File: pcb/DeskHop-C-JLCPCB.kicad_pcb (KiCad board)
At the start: 2 copper layers, 66.9 x 74.5 mm, 94 parts, among them J201 Debug, J202 Computer, J203 Power, J204 Device, J301 Debug, J302 Computer, J303 Power, J304 Device, Q201 USB Power Switch, Q301 USB Power Switch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

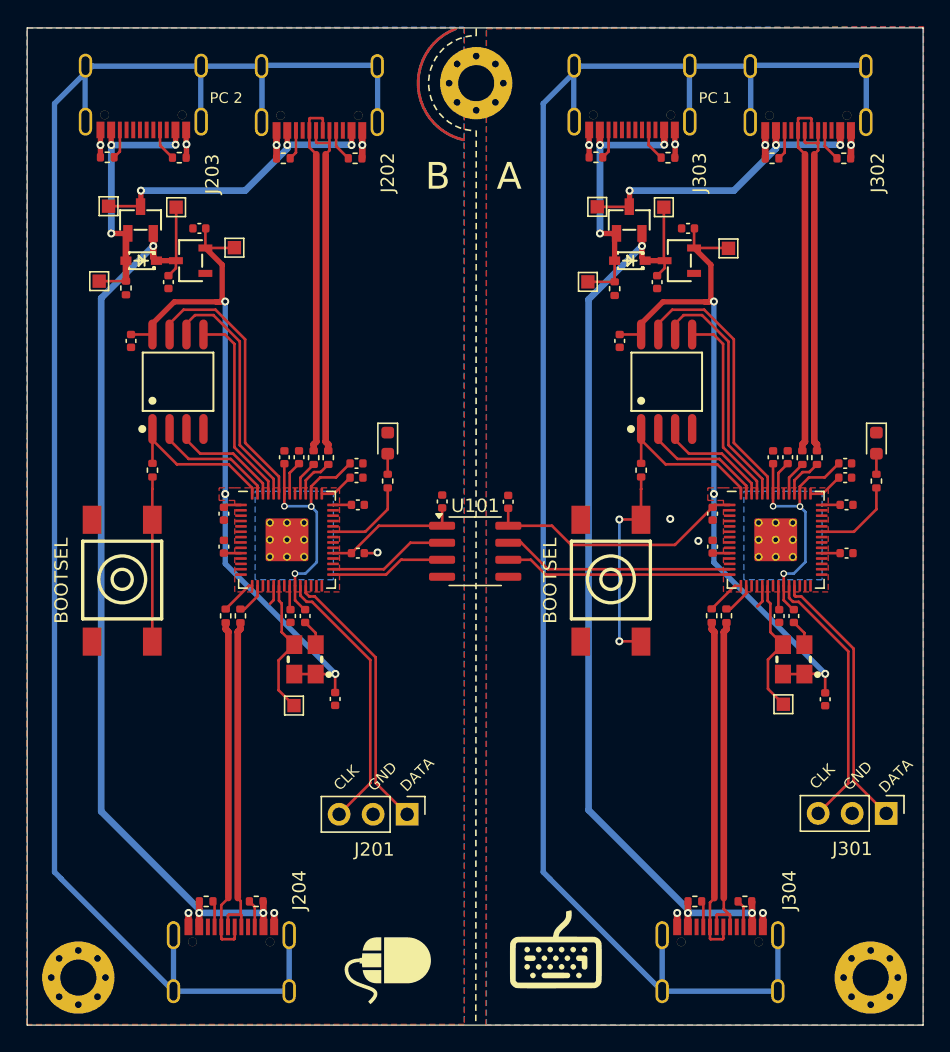
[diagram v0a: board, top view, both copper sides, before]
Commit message: Relocate various items to improve silkscreen placement.
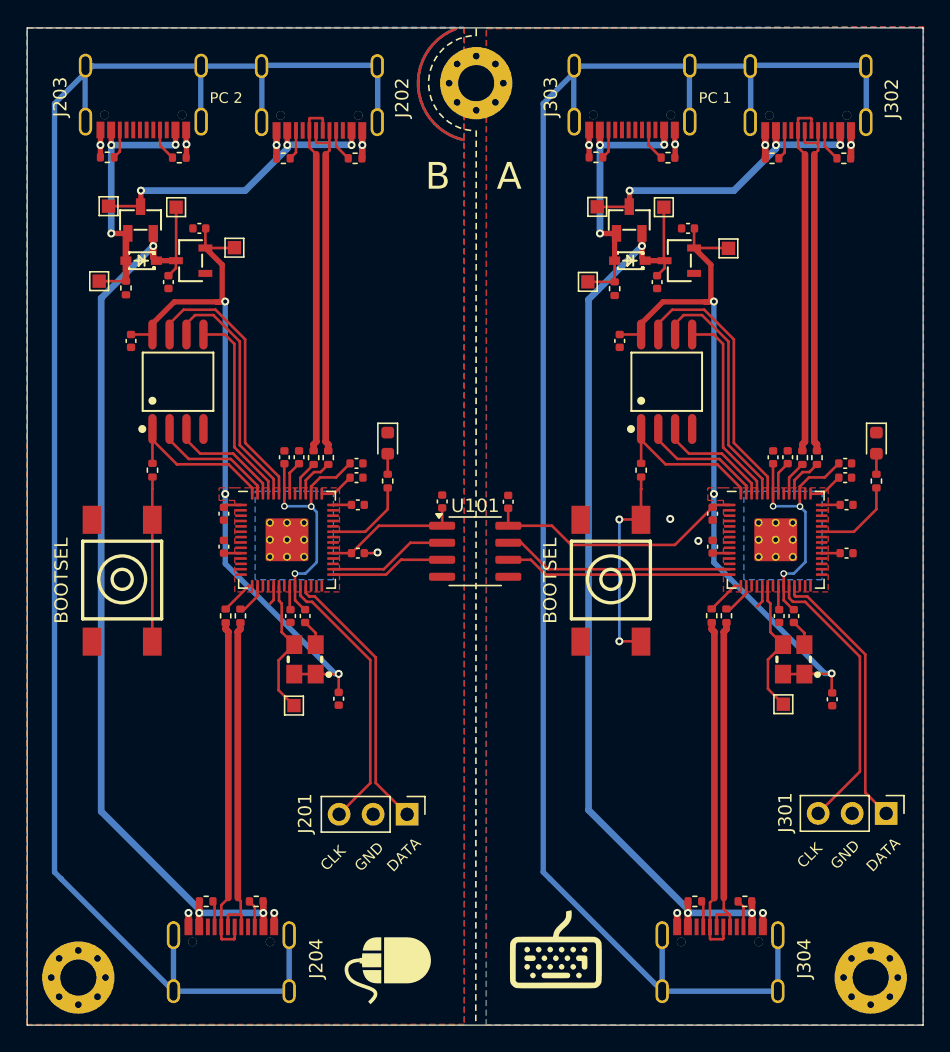
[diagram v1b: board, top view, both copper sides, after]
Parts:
- moved C302 0.53 mm to (93.9, 91.2)
- moved C202 0.27 mm to (57.0, 91.2)
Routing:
- net /Core Right (A)/3V3: track 82.6 -> 83.6 mm
- net Net-(J301-Pin_3): track 20.0 -> 21.0 mm

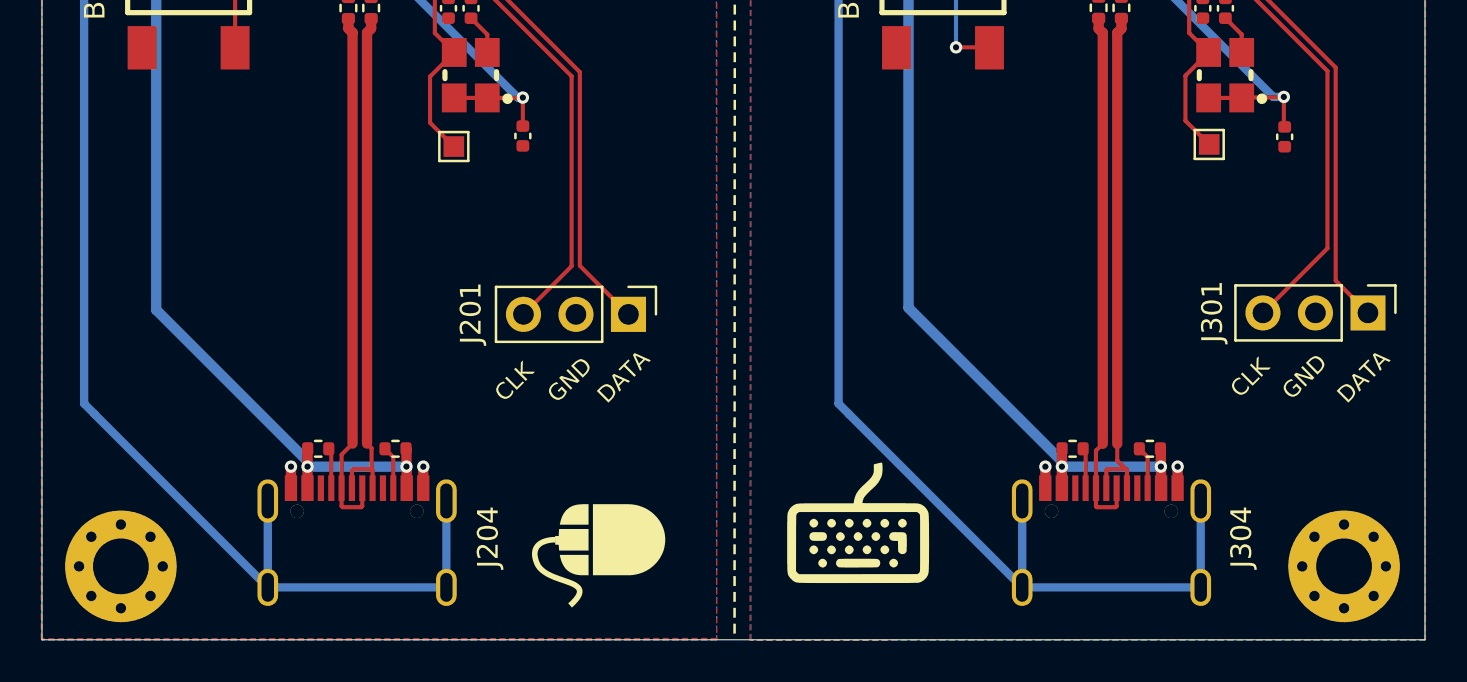
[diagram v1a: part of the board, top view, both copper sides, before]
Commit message: Adjust mounting hole positions to match original board.
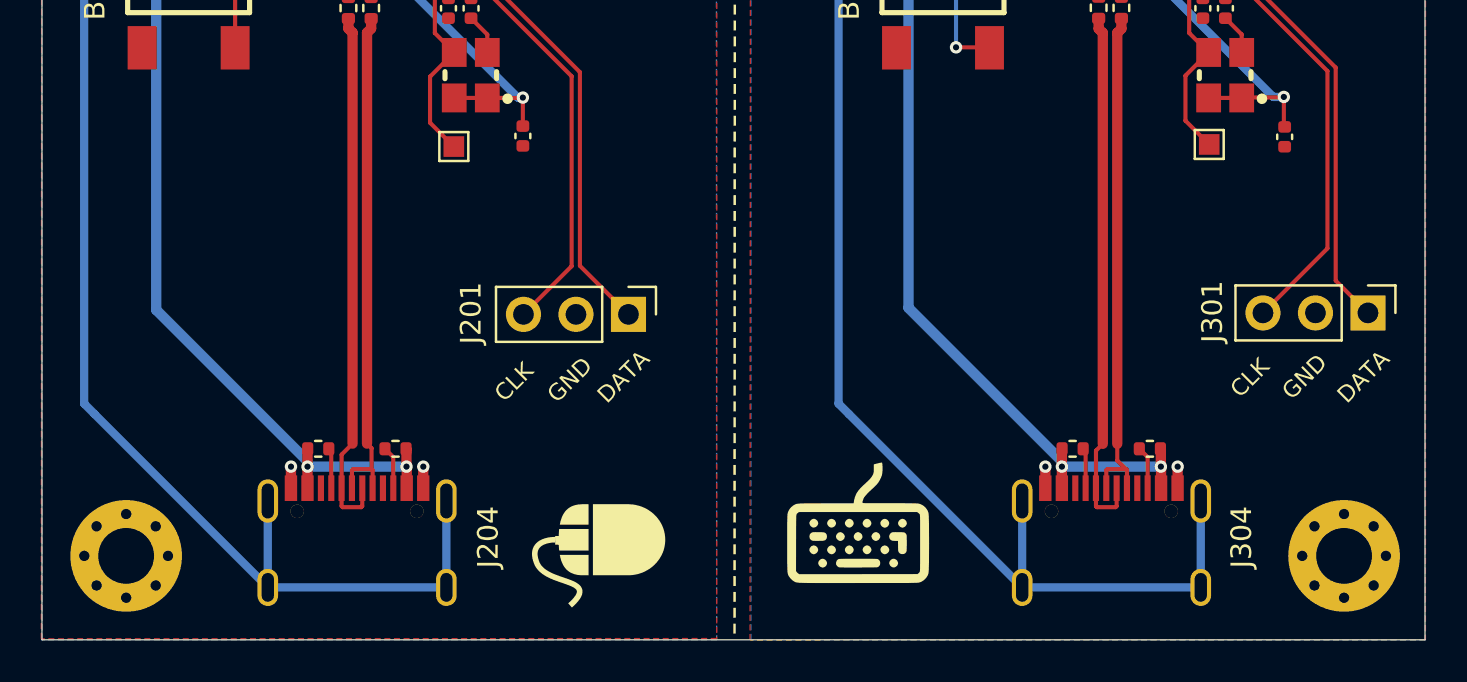
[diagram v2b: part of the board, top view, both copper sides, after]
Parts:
- moved H102 0.57 mm to (37.8, 111.5)
- moved H103 0.51 mm to (96.8, 111.5)
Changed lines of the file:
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@@
   )
   (footprint "MountingHole:MountingHole_2.7mm_M2.5_Pad_Via" (layer "F.Cu")
-    (at 37.592 112.014)
+    (at 37.846 111.506)
     (descr "Mounting Hole 2.7mm")
     (tags "mounting hole 2.7mm")
@@
   )
   (footprint "MountingHole:MountingHole_2.7mm_M2.5_Pad_Via" (layer "F.Cu")
-    (at 96.774 112.014)
+    (at 96.774 111.506)
     (descr "Mounting Hole 2.7mm")
     (tags "mounting hole 2.7mm")
@@
   (segment (start 93.1159 80.3157) (end 94.3805 80.3157) (width 0.2) (layer "F.Cu") (net 3))
   (segment (start 86.2409 80.3157) (end 84.9667 80.3157) (width 0.2) (layer "F.Cu") (net 3))
-  (segment (start 93.86 90.71) (end 93.9 90.75) (width 0.2) (layer "F.Cu") (net 3))
   (segment (start 86.2409 76.7157) (end 85.1359 76.7157) (width 0.2) (layer "F.Cu") (net 3))
   (segment (start 69.7 76.96) (end 69.7 78.2598) (width 0.2) (layer "F.Cu") (net 3))

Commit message: Use better net labels for UART links.
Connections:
- net /Core Left (B)/UART-RX-A renamed /Core Left (B)/RIGHT-UART-RX
- net /Core Left (B)/UART-RX-B renamed /Core Left (B)/LEFT-UART-RX
- net /Core Left (B)/UART-TX-A renamed /Core Left (B)/RIGHT-UART-TX
- net /Core Left (B)/UART-TX-B renamed /Core Left (B)/LEFT-UART-TX
- net /Core Right (A)/UART-RX-A renamed /Core Right (A)/RIGHT-UART-RX
- net /Core Right (A)/UART-RX-B renamed /Core Right (A)/LEFT-UART-RX
- net /Core Right (A)/UART-TX-A renamed /Core Right (A)/RIGHT-UART-TX
- net /Core Right (A)/UART-TX-B renamed /Core Right (A)/LEFT-UART-TX
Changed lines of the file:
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@@
   (net 59 "Net-(U303-GPIO13)")
   (net 60 "Net-(U303-GPIO12)")
-  (net 61 "/Core Left (B)/UART-RX-B")
-  (net 62 "/Core Left (B)/UART-TX-B")
-  (net 63 "/Core Right (A)/UART-RX-A")
-  (net 64 "/Core Right (A)/UART-TX-A")
+  (net 61 "/Core Left (B)/LEFT-UART-RX")
+  (net 62 "/Core Left (B)/LEFT-UART-TX")
+  (net 63 "/Core Right (A)/RIGHT-UART-RX")
+  (net 64 "/Core Right (A)/RIGHT-UART-TX")
   (net 65 "/Core Left (B)/QSPI_D0")
   (net 66 "/Core Left (B)/QSPI_D2")
@@
   (net 78 "unconnected-(U203-GPIO8-Pad11)")
   (net 79 "unconnected-(U203-GPIO9-Pad12)")
-  (net 80 "/Core Left (B)/UART-TX-A")
-  (net 81 "/Core Left (B)/UART-RX-A")
+  (net 80 "/Core Left (B)/RIGHT-UART-TX")
+  (net 81 "/Core Left (B)/RIGHT-UART-RX")
   (net 82 "unconnected-(U203-GPIO14-Pad17)")
   (net 83 "unconnected-(U203-GPIO15-Pad18)")
@@
   (net 116 "unconnected-(U303-GPIO16-Pad27)")
   (net 117 "unconnected-(U303-GPIO17-Pad28)")
-  (net 118 "/Core Right (A)/UART-TX-B")
-  (net 119 "/Core Right (A)/UART-RX-B")
+  (net 118 "/Core Right (A)/LEFT-UART-TX")
+  (net 119 "/Core Right (A)/LEFT-UART-RX")
   (net 120 "unconnected-(U303-GPIO20-Pad31)")
   (net 121 "unconnected-(U303-GPIO21-Pad32)")
@@
       (net 1 "/Core Left (B)/3V3") (pinfunction "VDD1") (pintype "power_in"))
     (pad "2" smd roundrect (at -2.475 -0.635) (size 1.95 0.6) (layers "F.Cu" "F.Paste" "F.Mask") (roundrect_rratio 0.25)
-      (net 61 "/Core Left (B)/UART-RX-B") (pinfunction "VOA") (pintype "output"))
+      (net 61 "/Core Left (B)/LEFT-UART-RX") (pinfunction "VOA") (pintype "output"))
     (pad "3" smd roundrect (at -2.475 0.635) (size 1.95 0.6) (layers "F.Cu" "F.Paste" "F.Mask") (roundrect_rratio 0.25)
-      (net 62 "/Core Left (B)/UART-TX-B") (pinfunction "VIB") (pintype "input"))
+      (net 62 "/Core Left (B)/LEFT-UART-TX") (pinfunction "VIB") (pintype "input"))
     (pad "4" smd roundrect (at -2.475 1.905) (size 1.95 0.6) (layers "F.Cu" "F.Paste" "F.Mask") (roundrect_rratio 0.25)
       (net 2 "/Core Left (B)/GND") (pinfunction "GND1") (pintype "power_in"))
@@
       (net 4 "/Core Right (A)/GND") (pinfunction "GND2") (pintype "power_in"))
     (pad "6" smd roundrect (at 2.475 0.635) (size 1.95 0.6) (layers "F.Cu" "F.Paste" "F.Mask") (roundrect_rratio 0.25)
-      (net 63 "/Core Right (A)/UART-RX-A") (pinfunction "VOB") (pintype "output"))
+      (net 63 "/Core Right (A)/RIGHT-UART-RX") (pinfunction "VOB") (pintype "output"))
     (pad "7" smd roundrect (at 2.475 -0.635) (size 1.95 0.6) (layers "F.Cu" "F.Paste" "F.Mask") (roundrect_rratio 0.25)
-      (net 64 "/Core Right (A)/UART-TX-A") (pinfunction "VIA") (pintype "input"))
+      (net 64 "/Core Right (A)/RIGHT-UART-TX") (pinfunction "VIA") (pintype "input"))
     (pad "8" smd roundrect (at 2.475 -1.905) (size 1.95 0.6) (layers "F.Cu" "F.Paste" "F.Mask") (roundrect_rratio 0.25)
       (net 3 "/Core Right (A)/3V3") (pinfunction "VDD2") (pintype "power_in"))
@@
       (net 79 "unconnected-(U203-GPIO9-Pad12)") (pinfunction "GPIO9") (pintype "bidirectional+no_connect"))
     (pad "13" smd roundrect (at -3.4375 2.2) (size 0.875 0.2) (layers "F.Cu" "F.Paste" "F.Mask") (roundrect_rratio 0.25)
-      (net 80 "/Core Left (B)/UART-TX-A") (pinfunction "GPIO10") (pintype "bidirectional+no_connect"))
+      (net 80 "/Core Left (B)/RIGHT-UART-TX") (pinfunction "GPIO10") (pintype "bidirectional+no_connect"))
     (pad "14" smd roundrect (at -3.4375 2.6) (size 0.875 0.2) (layers "F.Cu" "F.Paste" "F.Mask") (roundrect_rratio 0.25)
-      (net 81 "/Core Left (B)/UART-RX-A") (pinfunction "GPIO11") (pintype "bidirectional+no_connect"))
+      (net 81 "/Core Left (B)/RIGHT-UART-RX") (pinfunction "GPIO11") (pintype "bidirectional+no_connect"))
     (pad "15" smd roundrect (at -2.6 3.4375) (size 0.2 0.875) (layers "F.Cu" "F.Paste" "F.Mask") (roundrect_rratio 0.25)
       (net 54 "Net-(U203-GPIO12)") (pinfunction "GPIO12") (pintype "bidirectional"))
@@
       (net 87 "unconnected-(U203-GPIO17-Pad28)") (pinfunction "GPIO17") (pintype "bidirectional+no_connect"))
     (pad "29" smd roundrect (at 3.4375 2.6) (size 0.875 0.2) (layers "F.Cu" "F.Paste" "F.Mask") (roundrect_rratio 0.25)
-      (net 62 "/Core Left (B)/UART-TX-B") (pinfunction "GPIO18") (pintype "bidirectional"))
+      (net 62 "/Core Left (B)/LEFT-UART-TX") (pinfunction "GPIO18") (pintype "bidirectional"))
     (pad "30" smd roundrect (at 3.4375 2.2) (size 0.875 0.2) (layers "F.Cu" "F.Paste" "F.Mask") (roundrect_rratio 0.25)
-      (net 61 "/Core Left (B)/UART-RX-B") (pinfunction "GPIO19") (pintype "bidirectional"))
+      (net 61 "/Core Left (B)/LEFT-UART-RX") (pinfunction "GPIO19") (pintype "bidirectional"))
     (pad "31" smd roundrect (at 3.4375 1.8) (size 0.875 0.2) (layers "F.Cu" "F.Paste" "F.Mask") (roundrect_rratio 0.25)
       (net 88 "unconnected-(U203-GPIO20-Pad31)") (pinfunction "GPIO20") (pintype "bidirectional+no_connect"))
@@
       (net 111 "unconnected-(U303-GPIO9-Pad12)") (pinfunction "GPIO9") (pintype "bidirectional+no_connect"))
     (pad "13" smd roundrect (at -3.4375 2.2) (size 0.875 0.2) (layers "F.Cu" "F.Paste" "F.Mask") (roundrect_rratio 0.25)
-      (net 64 "/Core Right (A)/UART-TX-A") (pinfunction "GPIO10") (pintype "bidirectional"))
+      (net 64 "/Core Right (A)/RIGHT-UART-TX") (pinfunction "GPIO10") (pintype "bidirectional"))
     (pad "14" smd roundrect (at -3.4375 2.6) (size 0.875 0.2) (layers "F.Cu" "F.Paste" "F.Mask") (roundrect_rratio 0.25)
-      (net 63 "/Core Right (A)/UART-RX-A") (pinfunction "GPIO11") (pintype "bidirectional"))
+      (net 63 "/Core Right (A)/RIGHT-UART-RX") (pinfunction "GPIO11") (pintype "bidirectional"))
     (pad "15" smd roundrect (at -2.6 3.4375) (size 0.2 0.875) (layers "F.Cu" "F.Paste" "F.Mask") (roundrect_rratio 0.25)
       (net 60 "Net-(U303-GPIO12)") (pinfunction "GPIO12") (pintype "bidirectional"))
@@
       (net 117 "unconnected-(U303-GPIO17-Pad28)") (pinfunction "GPIO17") (pintype "bidirectional+no_connect"))
     (pad "29" smd roundrect (at 3.4375 2.6) (size 0.875 0.2) (layers "F.Cu" "F.Paste" "F.Mask") (roundrect_rratio 0.25)
-      (net 118 "/Core Right (A)/UART-TX-B") (pinfunction "GPIO18") (pintype "bidirectional+no_connect"))
+      (net 118 "/Core Right (A)/LEFT-UART-TX") (pinfunction "GPIO18") (pintype "bidirectional+no_connect"))
     (pad "30" smd roundrect (at 3.4375 2.2) (size 0.875 0.2) (layers "F.Cu" "F.Paste" "F.Mask") (roundrect_rratio 0.25)
-      (net 119 "/Core Right (A)/UART-RX-B") (pinfunction "GPIO19") (pintype "bidirectional+no_connect"))
+      (net 119 "/Core Right (A)/LEFT-UART-RX") (pinfunction "GPIO19") (pintype "bidirectional+no_connect"))
     (pad "31" smd roundrect (at 3.4375 1.8) (size 0.875 0.2) (layers "F.Cu" "F.Paste" "F.Mask") (roundrect_rratio 0.25)
       (net 120 "unconnected-(U303-GPIO20-Pad31)") (pinfunction "GPIO20") (pintype "bidirectional+no_connect"))
